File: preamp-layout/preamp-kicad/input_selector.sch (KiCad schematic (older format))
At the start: 40 parts, among them J50 Conn_01x03_Female, J51 Conn_01x03_Male, J52 Conn_01x03_Male, J53 Conn_01x03_Male, J54 Conn_01x03_Male, J55 Conn_01x07_Female, J56 Conn_01x07_Female, J57 Conn_01x03_Male, J58 Conn_01x03_Male, J59 Conn_01x03_Female, J60 Conn_01x02_Male, J61 Conn_01x02_Male, J62 Conn_01x03_Female, J63 Conn_01x03_Female, K2 G6JU, K3 G6JU, K4 G6JU, K5 G6JU, K6 G6JU, K7 G6JU, K8 G6JU, U6 MCP23S17_SP, U7 ULN2003, U8 ULN2003

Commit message: Sheet cleanup
pin names reassigned, standardized. Organized sheets to reduce clutter, increase readability.
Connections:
- wire segments 234 -> 244
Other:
- moved on the sheet: K2A, K2B, K2C, K3A, K3B, K3C, K4A, K4B, K4C, K5A, K5B, K5C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

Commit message: I2C init commit
Changed design from using SPI interface to I2C interface, with exception of front LED array (SPI).
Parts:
- removed J50: Conn_01x03_Female, Connector_PinHeader_2.54mm:PinHeader_1x03_P2.54mm_Vertical, symbol Connector:Conn_01x03_Female
- removed U6: MCP23S17_SP, Package_SO:SOIC-28W_7.5x17.9mm_P1.27mm, symbol Interface_Expansion:MCP23S17_SP
- added J50: Conn_01x02_Female, symbol Connector:Conn_01x02_Female
- added U6: MCP23017_SO, Package_SO:SOIC-28W_7.5x17.9mm_P1.27mm, symbol Interface_Expansion:MCP23017_SO
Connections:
- net labels added: IO_SCL, IO_SDA
- net labels removed: CLK, MOSI, ~CS
- wire segments 244 -> 242
- no-connect marks 15 -> 14
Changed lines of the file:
@@
 Wire Wire Line
 	950  1700 950  1800
-Text HLabel 2850 2000 0    50   Input ~ 0
-CLK
-Text HLabel 2850 1900 0    50   Input ~ 0
-~CS
-Text HLabel 2850 2100 0    50   Input ~ 0
-MOSI
 Text Label 7000 1900 0    50   ~ 0
 IN_3_R+
@@
 Wire Wire Line
 	5100 3400 5250 3400
-$Comp
-L Connector:Conn_01x03_Female J?
-U 1 1 6152C395
-P 1800 1050
-AR Path="/5E607732/6152C395" Ref="J?"  Part="1"
-AR Path="/5E2D8DA2/6152C395" Ref="J50"  Part="1"
-F 0 "J50" H 1692 1243 50  0000 C CNN
-F 1 "Conn_01x03_Female" H 1828 985 50  0001 L CNN
-F 2 "Connector_PinHeader_2.54mm:PinHeader_1x03_P2.54mm_Vertical" H 1800 1050 50  0001 C CNN
-F 3 "~" H 1800 1050 50  0001 C CNN
-	1    1800 1050
-	-1   0    0    -1
-$EndComp
 Text HLabel 3600 4750 0    50   UnSpc ~ 0
 A_IN_1_L
@@
 NoConn ~ 2950 2500
 NoConn ~ 2950 2600
-NoConn ~ 2950 2200
 NoConn ~ 4350 2600
 NoConn ~ 4350 3500
@@
 	1    0    0    -1
 $EndComp
-$Comp
-L Interface_Expansion:MCP23S17_SP U?
-U 1 1 5E01AA66
-P 3650 2700
-AR Path="/5E01AA66" Ref="U?"  Part="1"
-AR Path="/5E2D8DA2/5E01AA66" Ref="U6"  Part="1"
-F 0 "U6" H 3950 3800 50  0000 C CNN
-F 1 "MCP23S17_SP" H 3950 3700 50  0000 C CNN
-F 2 "Package_SO:SOIC-28W_7.5x17.9mm_P1.27mm" H 3850 1700 50  0001 L CNN
-F 3 "http://ww1.microchip.com/downloads/en/DeviceDoc/20001952C.pdf" H 3850 1600 50  0001 L CNN
-	1    3650 2700
-	1    0    0    -1
-$EndComp
 Text GLabel 1850 1650 1    50   UnSpc ~ 0
 +5V
@@
 	1850 1750 1750 1750
 Wire Wire Line
-	2000 950  2100 950
-Wire Wire Line
-	2000 1050 2100 1050
-Wire Wire Line
-	2000 1150 2100 1150
-Wire Wire Line
 	2950 1900 2850 1900
 Wire Wire Line
 	2950 2000 2850 2000
-Wire Wire Line
-	2950 2100 2850 2100
-Text HLabel 2100 1050 2    50   Input ~ 0
-CLK
-Text HLabel 2100 950  2    50   Input ~ 0
-~CS
-Text HLabel 2100 1150 2    50   Input ~ 0
-MOSI
 Text HLabel 1600 4150 2    50   UnSpc ~ 0
 A_IN_1_L
@@
 	0    1    1    0
 $EndComp
+$Comp
+L Interface_Expansion:MCP23017_SO U6
+U 1 1 61F87816
+P 3650 2700
+F 0 "U6" H 3950 3800 50  0000 C CNN
+F 1 "MCP23017_SO" H 3950 3700 50  0000 C CNN
+F 2 "Package_SO:SOIC-28W_7.5x17.9mm_P1.27mm" H 3850 1700 50  0001 L CNN
+F 3 "http://ww1.microchip.com/downloads/en/DeviceDoc/20001952C.pdf" H 3850 1600 50  0001 L CNN
+	1    3650 2700
+	1    0    0    -1
+$EndComp
+$Comp
+L Connector:Conn_01x02_Female J50
+U 1 1 61FF179F
+P 2650 1100
+F 0 "J50" H 2542 1193 50  0000 C CNN
+F 1 "Conn_01x02_Female" H 2542 1194 50  0001 C CNN
+F 2 "" H 2650 1100 50  0001 C CNN
+F 3 "~" H 2650 1100 50  0001 C CNN
+	1    2650 1100
+	-1   0    0    -1
+$EndComp
+Text HLabel 2900 1100 2    50   Input ~ 0
+IO_SDA
+Text HLabel 2900 1200 2    50   Input ~ 0
+IO_SCL
+Wire Wire Line
+	2850 1100 2900 1100
+Wire Wire Line
+	2850 1200 2900 1200
+Text HLabel 2850 1900 0    50   Input ~ 0
+IO_SDA
+Text HLabel 2850 2000 0    50   Input ~ 0
+IO_SCL
 $EndSCHEMATC

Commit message: BOM Update
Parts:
- renumbered J53 to J52, J52 to J53, J57 to J55, J55 to J56, J56 to J57
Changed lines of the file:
@@
 Wire Wire Line
 	2900 3500 2900 3850
-Text GLabel 2800 2800 0    50   UnSpc ~ 0
+Text GLabel 2850 2800 0    50   UnSpc ~ 0
 +5V
-Wire Wire Line
-	2800 2800 2950 2800
 Text GLabel 950  900  1    50   UnSpc ~ 0
 +5V
@@
 	5250 3800 5950 3800
 $Comp
-L Connector:Conn_01x07_Female J55
+L Connector:Conn_01x07_Female J56
 U 1 1 60FF250B
 P 4750 1150
-F 0 "J55" V 4823 1130 50  0000 C CNN
+F 0 "J56" V 4823 1130 50  0000 C CNN
 F 1 "Conn_01x07_Female" V 4824 1130 50  0001 C CNN
 F 2 "" H 4750 1150 50  0001 C CNN
@@
 	5050 2500 5850 2500
 $Comp
-L Connector:Conn_01x07_Female J56
+L Connector:Conn_01x07_Female J57
 U 1 1 610AC3C4
 P 4800 4000
-F 0 "J56" V 4873 3980 50  0000 C CNN
+F 0 "J57" V 4873 3980 50  0000 C CNN
 F 1 "Conn_01x07_Female" V 4874 3980 50  0001 C CNN
 F 2 "" H 4800 4000 50  0001 C CNN
@@
 $EndComp
 $Comp
-L Connector:Conn_01x03_Male J53
+L Connector:Conn_01x03_Male J52
 U 1 1 63D9CD4B
 P 1300 4750
-F 0 "J53" H 1200 4750 50  0000 C CNN
+F 0 "J52" H 1200 4750 50  0000 C CNN
 F 1 "Conn_01x03_Male" H 1272 4683 50  0001 R CNN
 F 2 "Connector_PinHeader_2.54mm:PinHeader_1x03_P2.54mm_Vertical" H 1300 4750 50  0001 C CNN
@@
 $EndComp
 $Comp
-L Connector:Conn_01x03_Male J57
+L Connector:Conn_01x03_Male J55
 U 1 1 63E64142
 P 1300 6250
-F 0 "J57" H 1200 6250 50  0000 C CNN
+F 0 "J55" H 1200 6250 50  0000 C CNN
 F 1 "Conn_01x03_Male" H 1272 6183 50  0001 R CNN
 F 2 "Connector_PinHeader_2.54mm:PinHeader_1x03_P2.54mm_Vertical" H 1300 6250 50  0001 C CNN
@@
 $EndComp
 $Comp
-L Connector:Conn_01x03_Male J52
+L Connector:Conn_01x03_Male J53
 U 1 1 63E1D8E7
 P 1300 5250
-F 0 "J52" H 1200 5250 50  0000 C CNN
+F 0 "J53" H 1200 5250 50  0000 C CNN
 F 1 "Conn_01x03_Male" H 1272 5183 50  0001 R CNN
 F 2 "Connector_PinHeader_2.54mm:PinHeader_1x03_P2.54mm_Vertical" H 1300 5250 50  0001 C CNN
@@
 Text HLabel 2850 2000 0    50   Input ~ 0
 IO_SCL
+Wire Wire Line
+	2850 2800 2950 2800
 $EndSCHEMATC

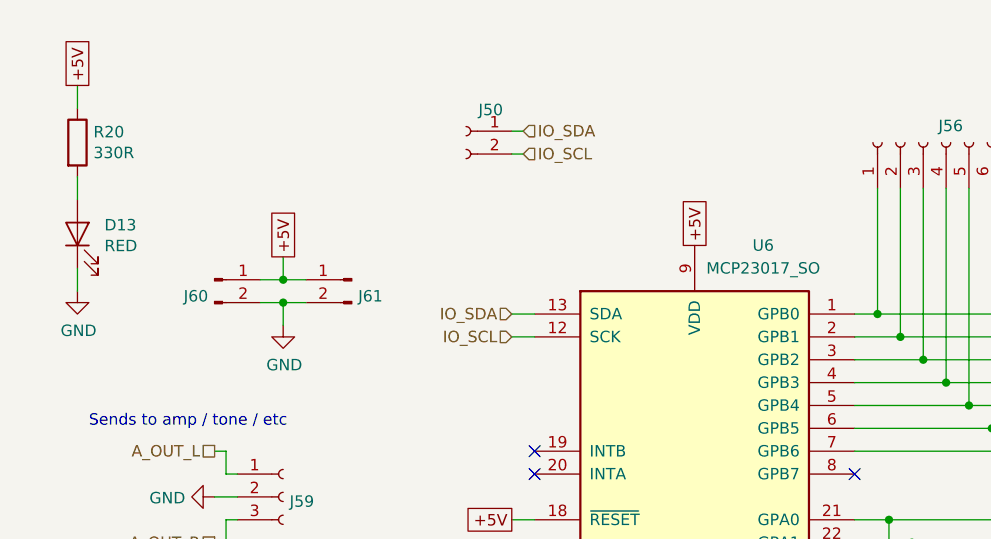
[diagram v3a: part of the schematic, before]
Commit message: Minor Updates
Moved headphone jack to amp pcb. I2C pin updates. Added caps to LED light strip. Added 0.1uF caps to all ICs.
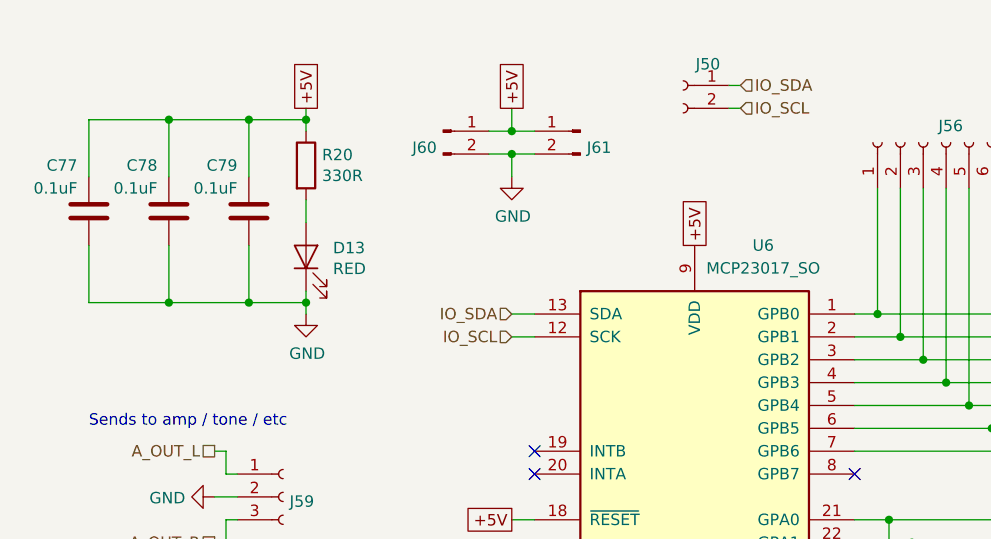
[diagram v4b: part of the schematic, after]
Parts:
- added C77, C78, C79: 0.1uF, Capacitor_SMD:C_0805_2012Metric_Pad1.15x1.40mm_HandSolder, symbol Device:C
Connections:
- net +5V: now also C77.1, C78.1, C79.1
- net GND: now also C77.2, C78.2, C79.2
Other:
- moved on the sheet: D13, J50, J60, J61, R20
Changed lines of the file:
@@
 $Descr A4 11693 8268
 encoding utf-8
-Sheet 8 13
+Sheet 7 13
 Title "IO Relay Select Board"
 Date "2020-02-25"
@@
 Text GLabel 2850 2800 0    50   UnSpc ~ 0
 +5V
-Text GLabel 950  900  1    50   UnSpc ~ 0
-+5V
-$Comp
-L Device:R R20
-U 1 1 5FDEBED2
-P 950 1150
-AR Path="/5E2D8DA2/5FDEBED2" Ref="R20"  Part="1"
-AR Path="/5FDEBED2" Ref="R?"  Part="1"
-F 0 "R20" H 1020 1196 50  0000 L CNN
-F 1 "330R" H 1020 1105 50  0000 L CNN
-F 2 "Resistor_SMD:R_1206_3216Metric_Pad1.42x1.75mm_HandSolder" V 880 1150 50  0001 C CNN
-F 3 "~" H 950 1150 50  0001 C CNN
-	1    950  1150
-	1    0    0    -1
-$EndComp
-$Comp
-L Device:LED D13
-U 1 1 5FE4B18E
-P 950 1550
-F 0 "D13" V 989 1432 50  0000 R CNN
-F 1 "RED" V 898 1432 50  0000 R CNN
-F 2 "LED_SMD:LED_1206_3216Metric_Pad1.42x1.75mm_HandSolder" H 950 1550 50  0001 C CNN
-F 3 "~" H 950 1550 50  0001 C CNN
-	1    950  1550
-	0    -1   -1   0
-$EndComp
-Wire Wire Line
-	950  900  950  1000
-Wire Wire Line
-	950  1300 950  1400
-Wire Wire Line
-	950  1700 950  1800
 Text Label 7000 1900 0    50   ~ 0
 IN_3_R+
@@
 L Connector:Conn_01x02_Male J61
 U 1 1 60B85B38
-P 2150 1750
-F 0 "J61" H 2122 1678 50  0000 R CNN
-F 1 "Conn_01x02_Male" H 2122 1633 50  0001 R CNN
-F 2 "Connector_JST:JST_EH_B2B-EH-A_1x02_P2.50mm_Vertical" H 2150 1750 50  0001 C CNN
-F 3 "~" H 2150 1750 50  0001 C CNN
-	1    2150 1750
+P 3150 1100
+F 0 "J61" H 3122 1028 50  0000 R CNN
+F 1 "Conn_01x02_Male" H 3122 983 50  0001 R CNN
+F 2 "Connector_JST:JST_EH_B2B-EH-A_1x02_P2.50mm_Vertical" H 3150 1100 50  0001 C CNN
+F 3 "~" H 3150 1100 50  0001 C CNN
+	1    3150 1100
 	-1   0    0    -1
 $EndComp
@@
 F 3 "" H 6350 4000 50  0001 C CNN
 	1    6350 4000
-	1    0    0    -1
-$EndComp
-$Comp
-L power:GND #PWR?
-U 1 1 64C5F5F4
-P 950 1800
-AR Path="/5E26F6FE/64C5F5F4" Ref="#PWR?"  Part="1"
-AR Path="/5E2D8DA2/64C5F5F4" Ref="#PWR061"  Part="1"
-F 0 "#PWR061" H 950 1550 50  0001 C CNN
-F 1 "GND" H 955 1627 50  0000 C CNN
-F 2 "" H 950 1800 50  0001 C CNN
-F 3 "" H 950 1800 50  0001 C CNN
-	1    950  1800
 	1    0    0    -1
 $EndComp
@@
 L Connector:Conn_01x02_Male J60
 U 1 1 5E5DB820
-P 1550 1750
-F 0 "J60" H 1522 1678 50  0000 R CNN
-F 1 "Conn_01x02_Male" H 1522 1633 50  0001 R CNN
-F 2 "Connector_JST:JST_EH_B2B-EH-A_1x02_P2.50mm_Vertical" H 1550 1750 50  0001 C CNN
-F 3 "~" H 1550 1750 50  0001 C CNN
-	1    1550 1750
+P 2550 1100
+F 0 "J60" H 2522 1028 50  0000 R CNN
+F 1 "Conn_01x02_Male" H 2522 983 50  0001 R CNN
+F 2 "Connector_JST:JST_EH_B2B-EH-A_1x02_P2.50mm_Vertical" H 2550 1100 50  0001 C CNN
+F 3 "~" H 2550 1100 50  0001 C CNN
+	1    2550 1100
 	1    0    0    -1
 $EndComp
@@
 	1    0    0    -1
 $EndComp
-Text GLabel 1850 1650 1    50   UnSpc ~ 0
+Text GLabel 2850 1000 1    50   UnSpc ~ 0
 +5V
 Wire Wire Line
-	1950 1850 1850 1850
-Wire Wire Line
-	1850 1850 1850 1950
-Wire Wire Line
-	1950 1750 1850 1750
+	2950 1200 2850 1200
+Wire Wire Line
+	2850 1200 2850 1300
+Wire Wire Line
+	2950 1100 2850 1100
 $Comp
 L power:GND #PWR?
 U 1 1 60248FFE
-P 1850 1950
+P 2850 1300
 AR Path="/6009D432/60248FFE" Ref="#PWR?"  Part="1"
 AR Path="/5E2D8DA2/60248FFE" Ref="#PWR0101"  Part="1"
-F 0 "#PWR0101" H 1850 1700 50  0001 C CNN
-F 1 "GND" H 1855 1777 50  0000 C CNN
-F 2 "" H 1850 1950 50  0001 C CNN
-F 3 "" H 1850 1950 50  0001 C CNN
-	1    1850 1950
-	1    0    0    -1
-$EndComp
-Connection ~ 1850 1850
-Wire Wire Line
-	1850 1850 1750 1850
-Wire Wire Line
-	1850 1650 1850 1750
-Connection ~ 1850 1750
-Wire Wire Line
-	1850 1750 1750 1750
+F 0 "#PWR0101" H 2850 1050 50  0001 C CNN
+F 1 "GND" H 2855 1127 50  0000 C CNN
+F 2 "" H 2850 1300 50  0001 C CNN
+F 3 "" H 2850 1300 50  0001 C CNN
+	1    2850 1300
+	1    0    0    -1
+$EndComp
+Connection ~ 2850 1200
+Wire Wire Line
+	2850 1200 2750 1200
+Wire Wire Line
+	2850 1000 2850 1100
+Connection ~ 2850 1100
+Wire Wire Line
+	2850 1100 2750 1100
 Wire Wire Line
 	2950 1900 2850 1900
@@
 L Connector:Conn_01x02_Female J50
 U 1 1 61FF179F
-P 2650 1100
-F 0 "J50" H 2542 1193 50  0000 C CNN
-F 1 "Conn_01x02_Female" H 2542 1194 50  0001 C CNN
-F 2 "" H 2650 1100 50  0001 C CNN
-F 3 "~" H 2650 1100 50  0001 C CNN
-	1    2650 1100
+P 3600 900
+F 0 "J50" H 3492 993 50  0000 C CNN
+F 1 "Conn_01x02_Female" H 3492 994 50  0001 C CNN
+F 2 "" H 3600 900 50  0001 C CNN
+F 3 "~" H 3600 900 50  0001 C CNN
+	1    3600 900
 	-1   0    0    -1
 $EndComp
-Text HLabel 2900 1100 2    50   Input ~ 0
+Text HLabel 3850 900  2    50   Input ~ 0
 IO_SDA
-Text HLabel 2900 1200 2    50   Input ~ 0
+Text HLabel 3850 1000 2    50   Input ~ 0
 IO_SCL
 Wire Wire Line
-	2850 1100 2900 1100
-Wire Wire Line
-	2850 1200 2900 1200
+	3800 900  3850 900
+Wire Wire Line
+	3800 1000 3850 1000
 Text HLabel 2850 1900 0    50   Input ~ 0
 IO_SDA
@@
 Wire Wire Line
 	2850 2800 2950 2800
+$Comp
+L Device:C C?
+U 1 1 5E93020B
+P 1350 1450
+AR Path="/5E4A803E/5E93020B" Ref="C?"  Part="1"
+AR Path="/6009D432/5E93020B" Ref="C?"  Part="1"
+AR Path="/5E5ECAAE/5E93020B" Ref="C?"  Part="1"
+AR Path="/5E2D8DA2/5E93020B" Ref="C78"  Part="1"
+F 0 "C78" H 1300 1650 50  0000 R CNN
+F 1 "0.1uF" H 1300 1550 50  0000 R CNN
+F 2 "Capacitor_SMD:C_0805_2012Metric_Pad1.15x1.40mm_HandSolder" H 1388 1300 50  0001 C CNN
+F 3 "~" H 1350 1450 50  0001 C CNN
+	1    1350 1450
+	1    0    0    -1
+$EndComp
+Wire Wire Line
+	1350 1600 1350 1850
+Wire Wire Line
+	1350 1300 1350 1050
+Wire Wire Line
+	1700 1850 1950 1850
+Wire Wire Line
+	1700 1050 1950 1050
+Wire Wire Line
+	1700 1600 1700 1850
+Wire Wire Line
+	1700 1300 1700 1050
+$Comp
+L power:GND #PWR?
+U 1 1 64C5F5F4
+P 1950 1900
+AR Path="/5E26F6FE/64C5F5F4" Ref="#PWR?"  Part="1"
+AR Path="/5E2D8DA2/64C5F5F4" Ref="#PWR061"  Part="1"
+F 0 "#PWR061" H 1950 1650 50  0001 C CNN
+F 1 "GND" H 1955 1727 50  0000 C CNN
+F 2 "" H 1950 1900 50  0001 C CNN
+F 3 "" H 1950 1900 50  0001 C CNN
+	1    1950 1900
+	1    0    0    -1
+$EndComp
+Wire Wire Line
+	1950 1800 1950 1850
+Wire Wire Line
+	1950 1400 1950 1500
+Wire Wire Line
+	1950 1000 1950 1050
+$Comp
+L Device:LED D13
+U 1 1 5FE4B18E
+P 1950 1650
+F 0 "D13" V 1989 1532 50  0000 R CNN
+F 1 "RED" V 1898 1532 50  0000 R CNN
+F 2 "LED_SMD:LED_1206_3216Metric_Pad1.42x1.75mm_HandSolder" H 1950 1650 50  0001 C CNN
+F 3 "~" H 1950 1650 50  0001 C CNN
+	1    1950 1650
+	0    -1   -1   0
+$EndComp
+$Comp
+L Device:R R20
+U 1 1 5FDEBED2
+P 1950 1250
+AR Path="/5E2D8DA2/5FDEBED2" Ref="R20"  Part="1"
+AR Path="/5FDEBED2" Ref="R?"  Part="1"
+F 0 "R20" H 2020 1296 50  0000 L CNN
+F 1 "330R" H 2020 1205 50  0000 L CNN
+F 2 "Resistor_SMD:R_1206_3216Metric_Pad1.42x1.75mm_HandSolder" V 1880 1250 50  0001 C CNN
+F 3 "~" H 1950 1250 50  0001 C CNN
+	1    1950 1250
+	1    0    0    -1
+$EndComp
+Text GLabel 1950 1000 1    50   UnSpc ~ 0
++5V
+Connection ~ 1950 1050
+Wire Wire Line
+	1950 1050 1950 1100
+Connection ~ 1950 1850
+Wire Wire Line
+	1950 1850 1950 1900
+Wire Wire Line
+	1000 1300 1000 1050
+Wire Wire Line
+	1000 1600 1000 1850
+$Comp
+L Device:C C?
+U 1 1 5E945AA6
+P 1000 1450
+AR Path="/5E4A803E/5E945AA6" Ref="C?"  Part="1"
+AR Path="/6009D432/5E945AA6" Ref="C?"  Part="1"
+AR Path="/5E5ECAAE/5E945AA6" Ref="C?"  Part="1"
+AR Path="/5E2D8DA2/5E945AA6" Ref="C77"  Part="1"
+F 0 "C77" H 950 1650 50  0000 R CNN
+F 1 "0.1uF" H 950 1550 50  0000 R CNN
+F 2 "Capacitor_SMD:C_0805_2012Metric_Pad1.15x1.40mm_HandSolder" H 1038 1300 50  0001 C CNN
+F 3 "~" H 1000 1450 50  0001 C CNN
+	1    1000 1450
+	1    0    0    -1
+$EndComp
+$Comp
+L Device:C C?
+U 1 1 5E91A99B
+P 1700 1450
+AR Path="/5E4A803E/5E91A99B" Ref="C?"  Part="1"
+AR Path="/6009D432/5E91A99B" Ref="C?"  Part="1"
+AR Path="/5E5ECAAE/5E91A99B" Ref="C?"  Part="1"
+AR Path="/5E2D8DA2/5E91A99B" Ref="C79"  Part="1"
+F 0 "C79" H 1650 1650 50  0000 R CNN
+F 1 "0.1uF" H 1650 1550 50  0000 R CNN
+F 2 "Capacitor_SMD:C_0805_2012Metric_Pad1.15x1.40mm_HandSolder" H 1738 1300 50  0001 C CNN
+F 3 "~" H 1700 1450 50  0001 C CNN
+	1    1700 1450
+	1    0    0    -1
+$EndComp
+Wire Wire Line
+	1000 1050 1350 1050
+Connection ~ 1350 1050
+Wire Wire Line
+	1000 1850 1350 1850
+Connection ~ 1350 1850
+Wire Wire Line
+	1350 1850 1700 1850
+Connection ~ 1700 1850
+Wire Wire Line
+	1350 1050 1700 1050
+Connection ~ 1700 1050
 $EndSCHEMATC
